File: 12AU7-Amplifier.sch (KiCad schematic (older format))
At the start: 29 parts, among them J1 SJ-3523N, J2 Barrel_Jack, J3 SJ-3523N, Q1 IRF510, Q2 IRF510, SW1 SW_SPDT, U1 12AU7, U2 LM317, U3 LM317

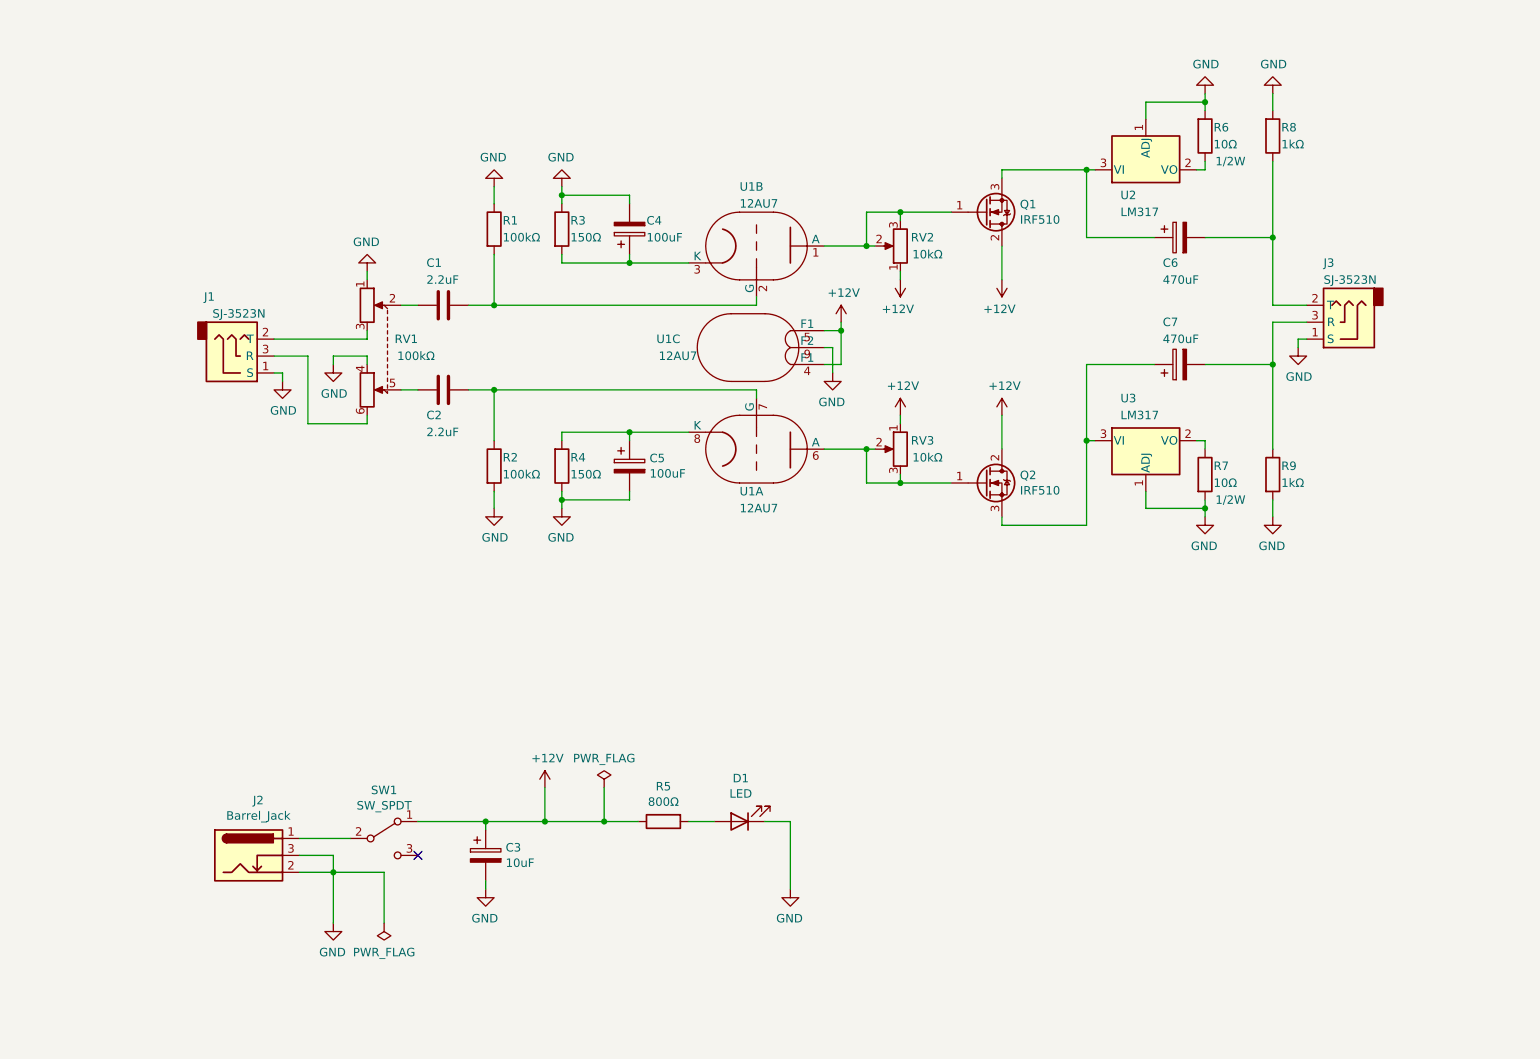
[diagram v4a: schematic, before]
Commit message: Fix resistor values, add parts list
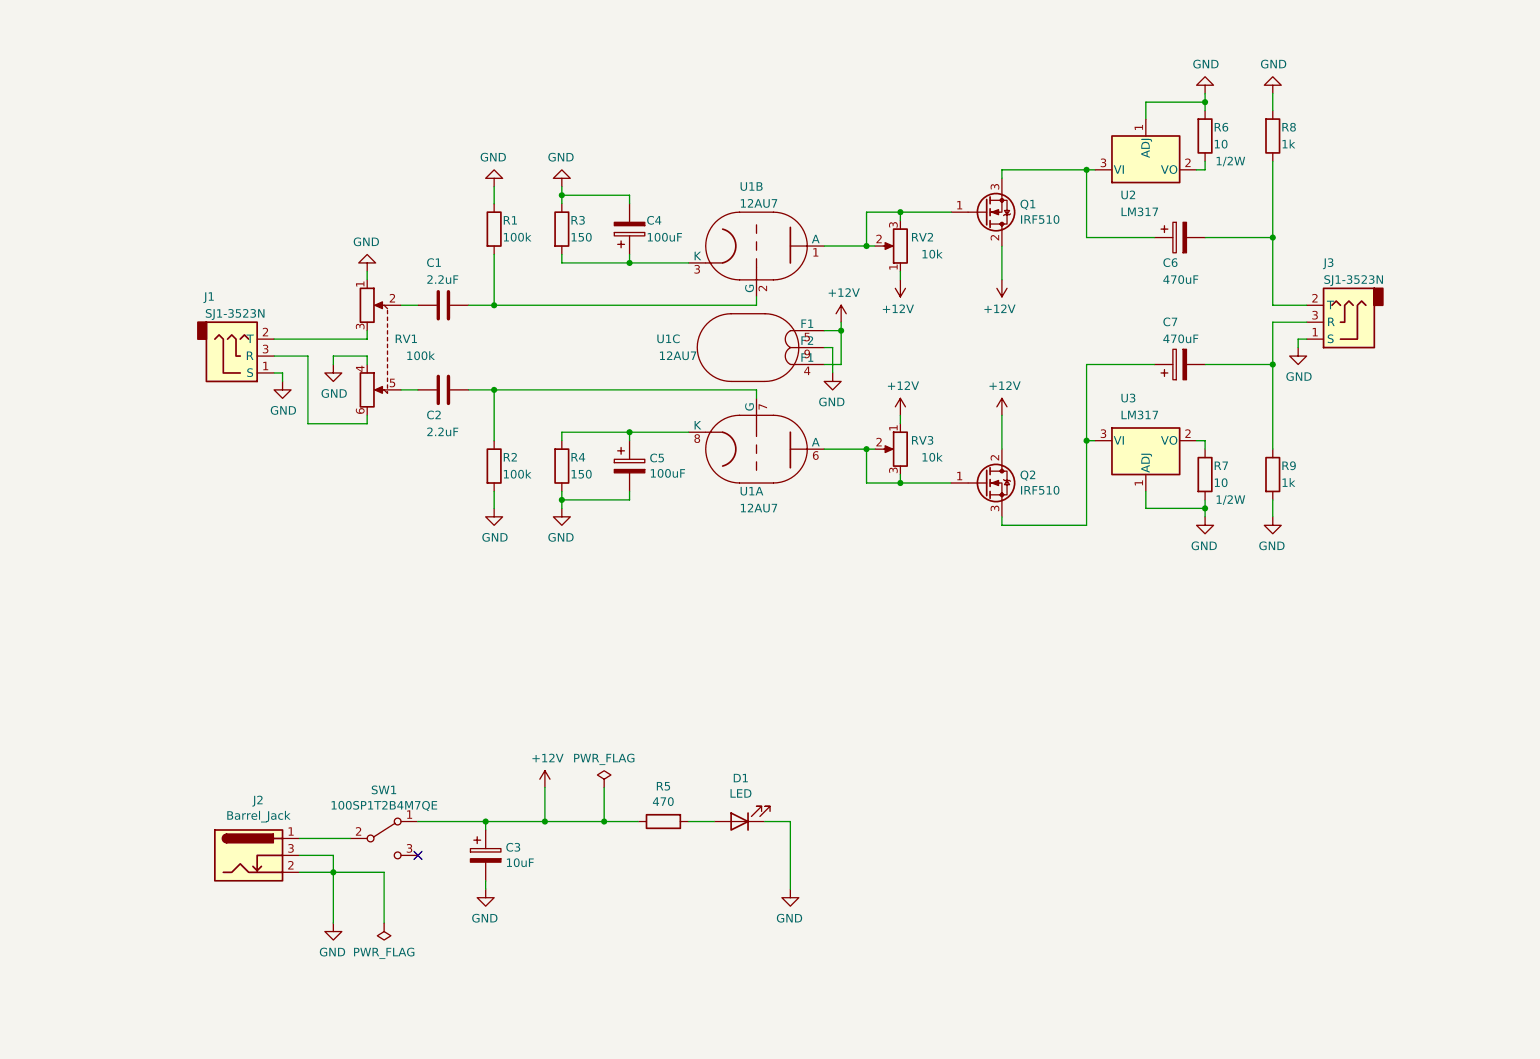
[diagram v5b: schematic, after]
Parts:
- J1, J3: value SJ-3523N -> SJ1-3523N
- R1, R2, RV1: value 100kΩ -> 100k
- R3, R4: value 150Ω -> 150
- R5: value 800Ω -> 470
- R6, R7: value 10Ω -> 10
- R8, R9: value 1kΩ -> 1k
- RV2, RV3: value 10kΩ -> 10k
- SW1: value SW_SPDT -> 100SP1T2B4M7QE
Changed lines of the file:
@@
 P 8000 1950
 F 0 "R6" H 8050 1900 50  0000 L CNN
-F 1 "10Ω" H 8050 2000 50  0000 L CNN
+F 1 "10" H 8050 2000 50  0000 L CNN
 F 2 "Resistor_THT:R_Axial_DIN0207_L6.3mm_D2.5mm_P10.16mm_Horizontal" V 7930 1950 50  0001 C CNN
 F 3 "~" H 8000 1950 50  0001 C CNN
@@
 P 8400 1950
 F 0 "R8" H 8450 1900 50  0000 L CNN
-F 1 "1kΩ" H 8450 2000 50  0000 L CNN
+F 1 "1k" H 8450 2000 50  0000 L CNN
 F 2 "Resistor_THT:R_Axial_DIN0207_L6.3mm_D2.5mm_P10.16mm_Horizontal" V 8330 1950 50  0001 C CNN
 F 3 "~" H 8400 1950 50  0001 C CNN
@@
 P 8000 3950
 F 0 "R7" H 8050 4000 50  0000 L CNN
-F 1 "10Ω" H 8050 3900 50  0000 L CNN
+F 1 "10" H 8050 3900 50  0000 L CNN
 F 2 "Resistor_THT:R_Axial_DIN0207_L6.3mm_D2.5mm_P10.16mm_Horizontal" V 7930 3950 50  0001 C CNN
 F 3 "~" H 8000 3950 50  0001 C CNN
@@
 P 6200 2600
 F 0 "RV2" H 6000 2550 50  0000 L CNN
-F 1 "10kΩ" H 5950 2650 50  0000 L CNN
+F 1 "10k" H 5950 2650 50  0000 L CNN
 F 2 "Potentiometer_THT:Potentiometer_Piher_PT-10-H01_Horizontal" H 6200 2600 50  0001 C CNN
 F 3 "~" H 6200 2600 50  0001 C CNN
@@
 P 3800 2500
 F 0 "R1" H 3850 2550 50  0000 L CNN
-F 1 "100kΩ" H 3850 2450 50  0000 L CNN
+F 1 "100k" H 3850 2450 50  0000 L CNN
 F 2 "Resistor_THT:R_Axial_DIN0207_L6.3mm_D2.5mm_P10.16mm_Horizontal" V 3730 2500 50  0001 C CNN
 F 3 "~" H 3800 2500 50  0001 C CNN
@@
 P 3800 3900
 F 0 "R2" H 3850 3950 50  0000 L CNN
-F 1 "100kΩ" H 3850 3850 50  0000 L CNN
+F 1 "100k" H 3850 3850 50  0000 L CNN
 F 2 "Resistor_THT:R_Axial_DIN0207_L6.3mm_D2.5mm_P10.16mm_Horizontal" V 3730 3900 50  0001 C CNN
 F 3 "~" H 3800 3900 50  0001 C CNN
@@
 P 8400 3950
 F 0 "R9" H 8450 4000 50  0000 L CNN
-F 1 "1kΩ" H 8450 3900 50  0000 L CNN
+F 1 "1k" H 8450 3900 50  0000 L CNN
 F 2 "Resistor_THT:R_Axial_DIN0207_L6.3mm_D2.5mm_P10.16mm_Horizontal" V 8330 3950 50  0001 C CNN
 F 3 "~" H 8400 3950 50  0001 C CNN
@@
 P 6200 3800
 F 0 "RV3" H 6000 3850 50  0000 L CNN
-F 1 "10kΩ" H 5950 3750 50  0000 L CNN
+F 1 "10k" H 5950 3750 50  0000 L CNN
 F 2 "Potentiometer_THT:Potentiometer_Piher_PT-10-H01_Horizontal" H 6200 3800 50  0001 C CNN
 F 3 "~" H 6200 3800 50  0001 C CNN
@@
 P 3150 3200
 F 0 "RV1" V 3100 3400 50  0000 R CNN
-F 1 "100kΩ" V 3200 3500 50  0000 R CNN
+F 1 "100k" V 3200 3500 50  0000 R CNN
 F 2 "12AU7-Amplifier:Alps_100KAX2" H 3400 3125 50  0001 C CNN
 F 3 "~" H 3400 3125 50  0001 C CNN
@@
 P 4200 3900
 F 0 "R4" H 4250 3850 50  0000 L CNN
-F 1 "150Ω" H 4250 3950 50  0000 L CNN
+F 1 "150" H 4250 3950 50  0000 L CNN
 F 2 "Resistor_THT:R_Axial_DIN0614_L14.3mm_D5.7mm_P5.08mm_Vertical" V 4130 3900 50  0001 C CNN
 F 3 "~" H 4200 3900 50  0001 C CNN
@@
 P 4200 2500
 F 0 "R3" H 4250 2550 50  0000 L CNN
-F 1 "150Ω" H 4250 2450 50  0000 L CNN
+F 1 "150" H 4250 2450 50  0000 L CNN
 F 2 "Resistor_THT:R_Axial_DIN0614_L14.3mm_D5.7mm_P5.08mm_Vertical" V 4130 2500 50  0001 C CNN
 F 3 "~" H 4200 2500 50  0001 C CNN
@@
 P 8800 3050
 F 0 "J3" H 8900 2700 50  0000 R CNN
-F 1 "SJ-3523N" H 8900 2800 50  0000 R CNN
+F 1 "SJ1-3523N" H 8900 2800 50  0000 R CNN
 F 2 "12AU7-Amplifier:Headphone_Jack_3.5mm_SJ1-3523N" H 8800 3050 50  0001 C CNN
 F 3 "https://www.cuidevices.com/product/resource/sj1-352xn.pdf" H 8800 3050 50  0001 C CNN
@@
 P 2300 3250
 F 0 "J1" H 2150 2900 50  0000 R CNN
-F 1 "SJ-3523N" H 2450 3000 50  0000 R CNN
+F 1 "SJ1-3523N" H 2450 3000 50  0000 R CNN
 F 2 "12AU7-Amplifier:Headphone_Jack_3.5mm_SJ1-3523N" H 2300 3250 50  0001 C CNN
 F 3 "https://www.cuidevices.com/product/resource/sj1-352xn.pdf" H 2300 3250 50  0001 C CNN
@@
 P 3150 6100
 F 0 "SW1" H 3150 6385 50  0000 C CNN
-F 1 "SW_SPDT" H 3150 6294 50  0000 C CNN
+F 1 "100SP1T2B4M7QE" H 3150 6294 50  0000 C CNN
 F 2 "12AU7-Amplifier:100SP1T2B4M7QE" H 3150 6100 50  0001 C CNN
 F 3 "~" H 3150 6100 50  0001 C CNN
@@
 P 4800 6000
 F 0 "R5" V 4593 6000 50  0000 C CNN
-F 1 "800Ω" V 4684 6000 50  0000 C CNN
+F 1 "470" V 4684 6000 50  0000 C CNN
 F 2 "Resistor_THT:R_Axial_DIN0207_L6.3mm_D2.5mm_P10.16mm_Horizontal" V 4730 6000 50  0001 C CNN
 F 3 "~" H 4800 6000 50  0001 C CNN

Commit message: Move step models to lib, added trimmer pot
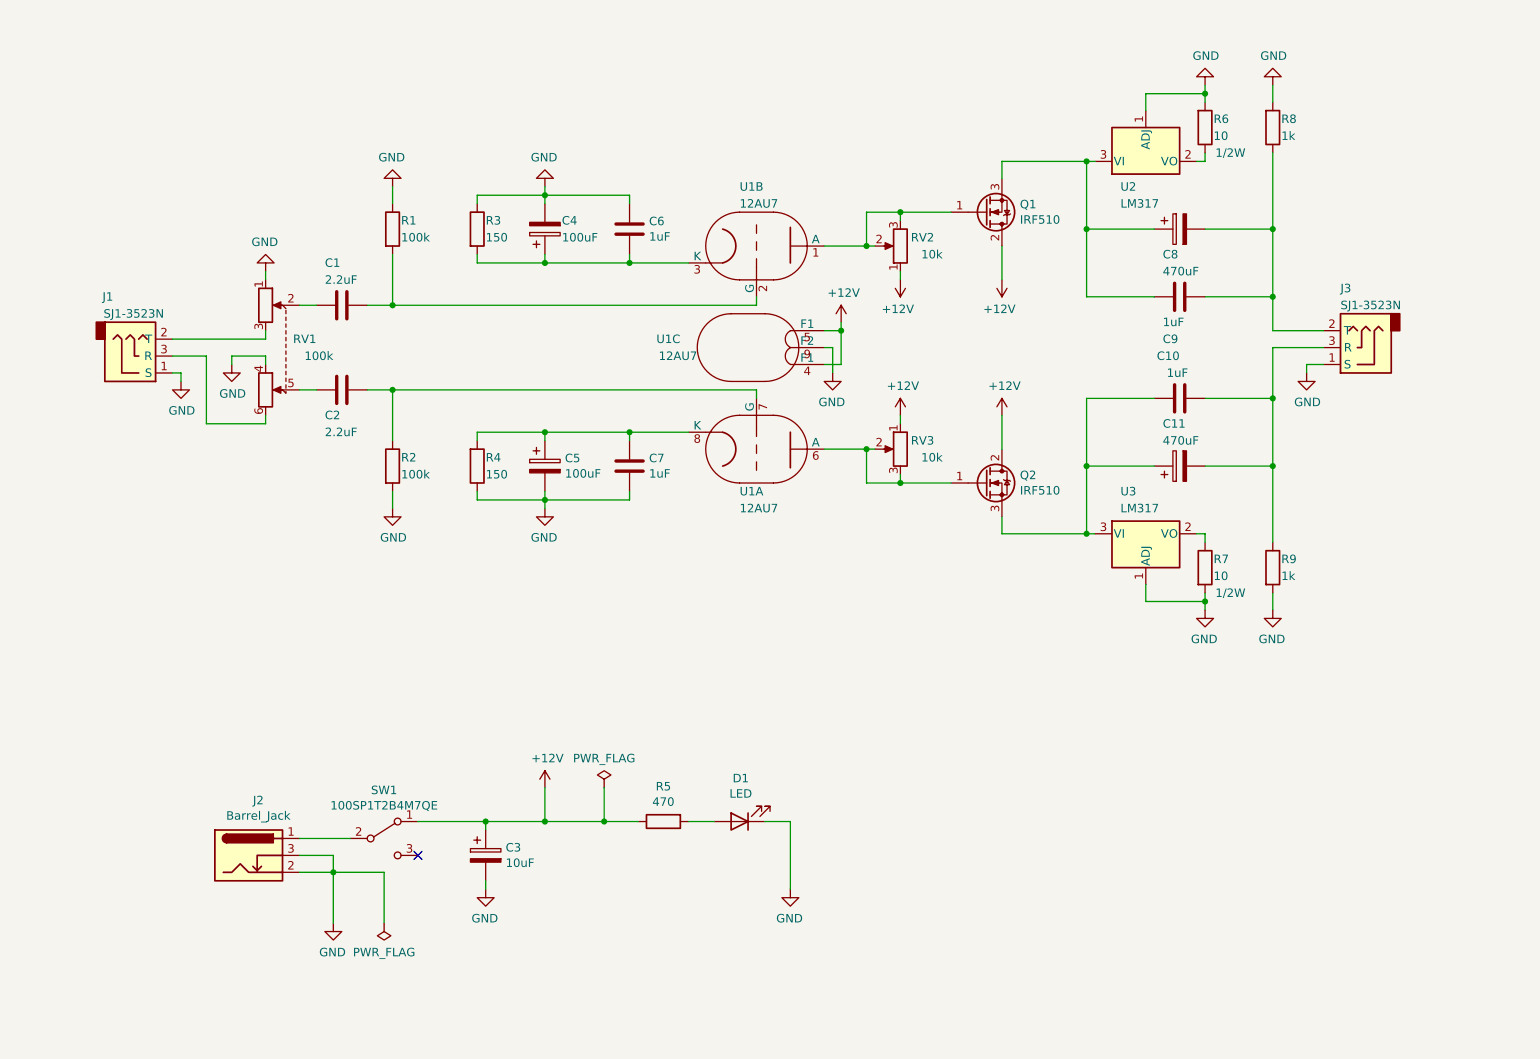
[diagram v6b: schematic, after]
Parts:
- added C10, C6, C7, C9: 1uF, Capacitor_THT:C_Rect_L18.0mm_W8.0mm_P15.00mm_FKS3_FKP3, symbol Device:C
- C1, C2: footprint Capacitor_THT:C_Radial_D5.0mm_H11.0mm_P2.00mm -> Capacitor_THT:C_Rect_L18.0mm_W11.0mm_P15.00mm_FKS3_FKP3
- C4, C5: footprint Capacitor_THT:CP_Radial_D8.0mm_P2.50mm -> Capacitor_THT:CP_Radial_D8.0mm_P3.50mm
- RV2, RV3: footprint Potentiometer_THT:Potentiometer_Piher_PT-10-H01_Horizontal -> 12AU7-Amplifier:CT6EP103
- renumbered C7 to C11, C6 to C8
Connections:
- net GND: now also C6.1, C7.2
- net at C4.1, R3.2, U1.3 (K): now also C6.2
- net at C11.1, Q2.3 (S), U3.3 (VI): now also C10.1
- net at C11.2, J3.3 (R), R9.1: now also C10.2
- net at C5.1, R4.2, U1.8 (K): now also C7.1
- net at C8.1, Q1.3 (S), U2.3 (VI): now also C9.2
- net at C8.2, J3.2 (T), R8.1: now also C9.1
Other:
- moved on the sheet: C1, C11, C2, C4, C5, C8, J1, J3, R1, R2, R3, R4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
